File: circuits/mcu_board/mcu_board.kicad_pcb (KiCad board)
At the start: 2 copper layers, 96.3 x 63.9 mm, 44 parts, among them J1 USB_B_Micro, J2 Conn_01x13_Pin, J3 Conn_01x03_Pin, SW1 SW_Push, SW10 SW_Push, SW11 SW_Push, SW12 SW_Push, SW13 SW_Push, SW2 SW_Push, SW3 SW_Push, SW4 SW_Push, SW5 SW_Push, SW6 SW_Push, SW7 SW_Push, SW8 SW_Push, SW9 SW_Push, U1 AMS1117-3.3, U4 STM32F103CBTx, Y1 8MHz

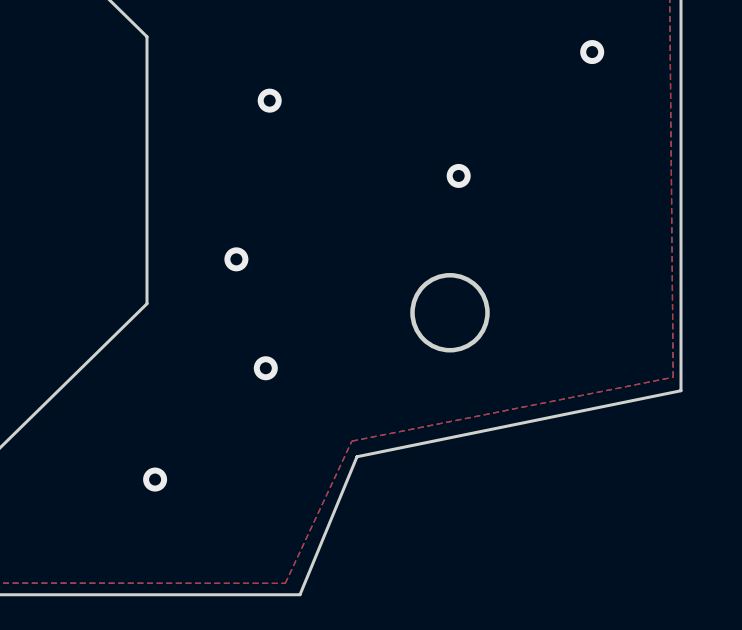
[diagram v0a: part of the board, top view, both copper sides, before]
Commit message: 微调螺丝孔
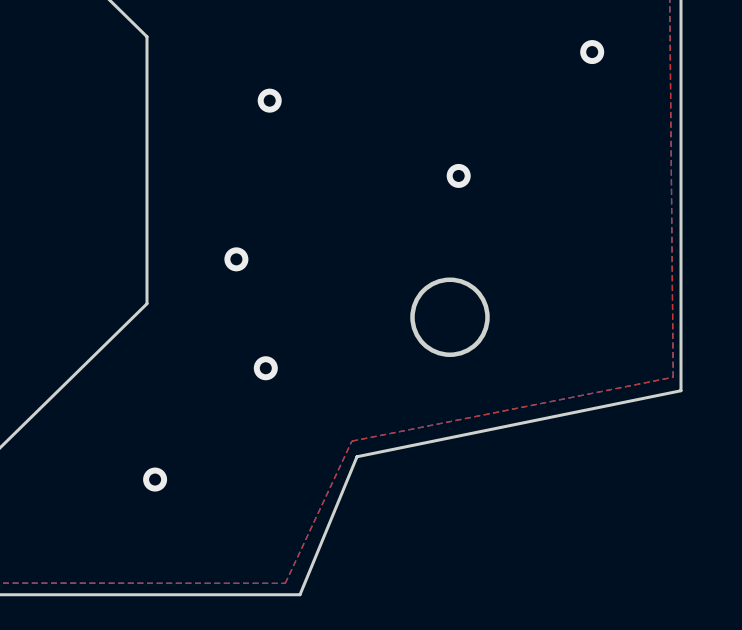
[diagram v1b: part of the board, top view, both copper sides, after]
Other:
- outline, holes or cut-outs redrawn

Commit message: not done
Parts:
- moved C2 7.83 mm to (150.6, 86.8), turned to -90 degrees
- moved C9 4.95 mm to (169.3, 116.7), turned to 90 degrees
- moved C8 4.94 mm to (170.2, 113.4)
- moved Y1 4.00 mm to (166.1, 114.9)
- moved U1 3.72 mm to (149.5, 96.0)
- moved U4 2.38 mm to (150.2, 115.7)
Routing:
- net +3V3: track 385.1 -> 363.9 mm, vias 15 -> 13
- net /BTN_B: track 22.0 -> 3.39 mm
- net Net-(U4-NRST): track 27.2 -> 8.86 mm, vias 2 -> 1
- net /RIGHT_BTN: track 21.5 -> 4.02 mm
- net /LEFT_BTN: track 24.0 -> 13.5 mm
- net VBUS: track 30.3 -> 24.8 mm
- net GND: track 265.9 -> 261.2 mm, vias 133 -> 121
- net /OSC_OUT: track 19.2 -> 16.5 mm, vias 2 -> 1
- net /BTN_LM: track 15.0 -> 17.5 mm
- net /BTN_X: track 58.8 -> 61.2 mm
- net /BTN_RM: track 38.9 -> 41.2 mm
- net Net-(U4-BOOT0): track 18.7 -> 21.0 mm
- net /LEFT_Y: track 13.4 -> 11.0 mm
- net /LEFT_X: track 13.5 -> 11.2 mm
- net /BTN_RB: track 43.8 -> 46.2 mm
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
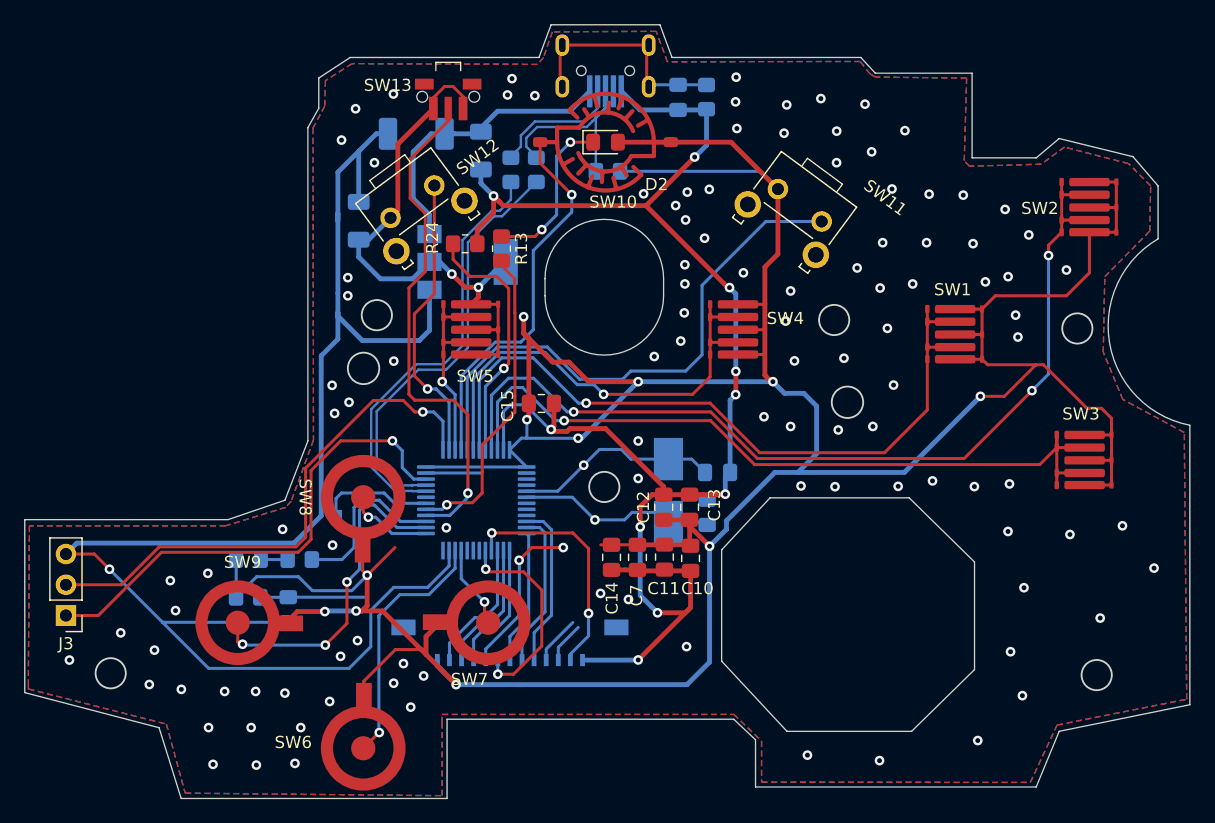
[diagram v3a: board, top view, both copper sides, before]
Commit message: 优化元件位置,防止外壳挤压
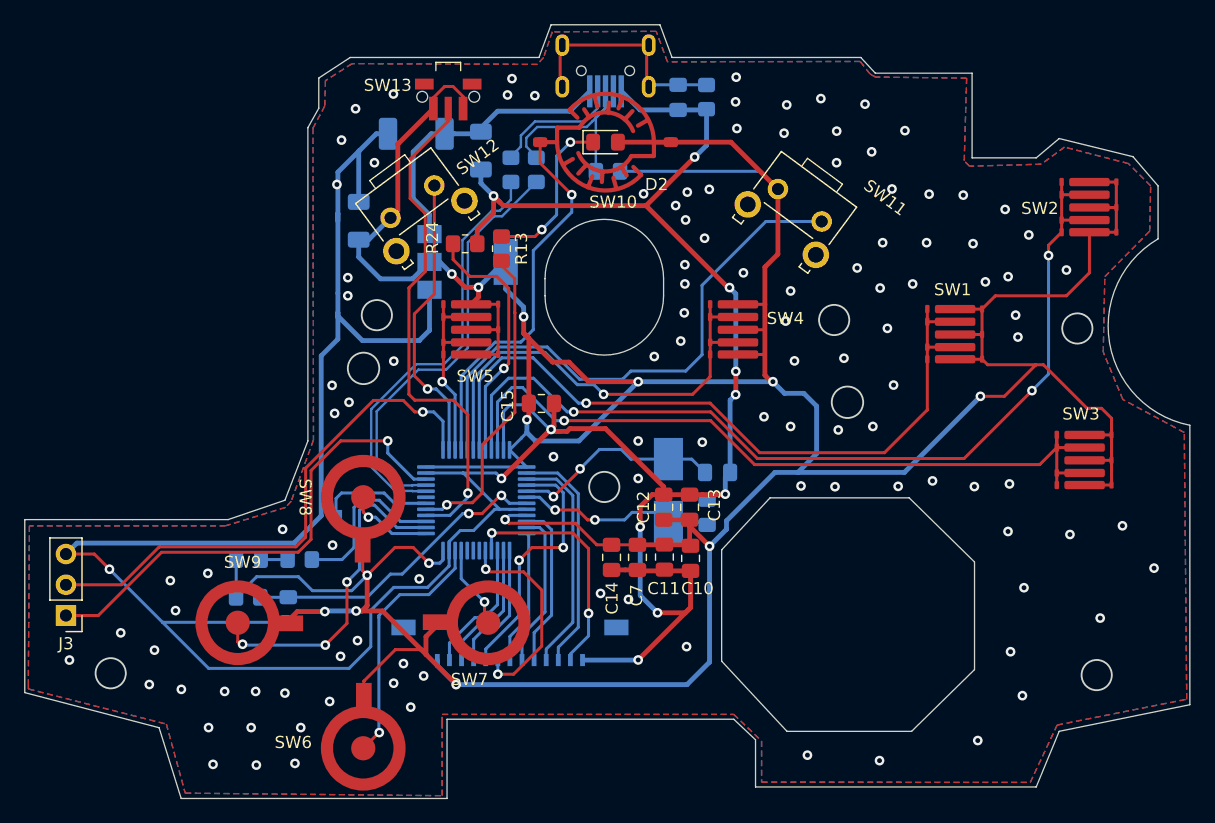
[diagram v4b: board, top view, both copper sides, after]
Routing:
- net +3V3: track 363.9 -> 385.0 mm, vias 13 -> 14
- net GND: track 261.2 -> 282.2 mm, vias 121 -> 126
- net Net-(U4-NRST): track 8.86 -> 25.8 mm, vias 1 -> 2
- net /BTN_B: track 3.39 -> 19.4 mm
- net /RIGHT_BTN: track 4.02 -> 18.9 mm
- net /LEFT_BTN: track 13.5 -> 21.3 mm
- net /OSC_IN: track 17.0 -> 17.4 mm, vias 1 -> 2
- net /OSC_OUT: track 16.5 -> 16.4 mm, vias 1 -> 2

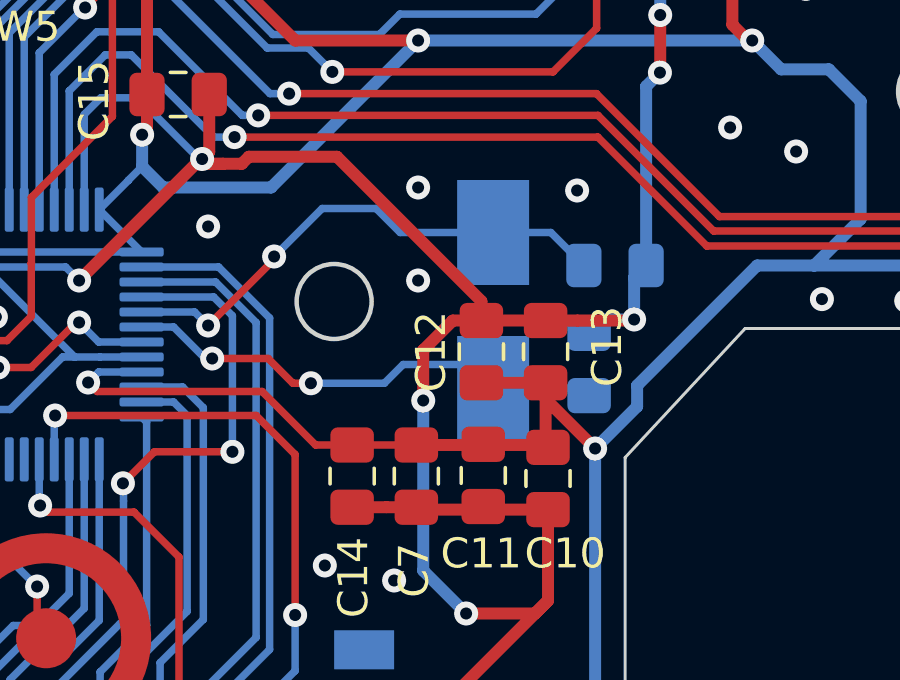
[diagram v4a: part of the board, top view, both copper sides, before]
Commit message: 晶振下移一点
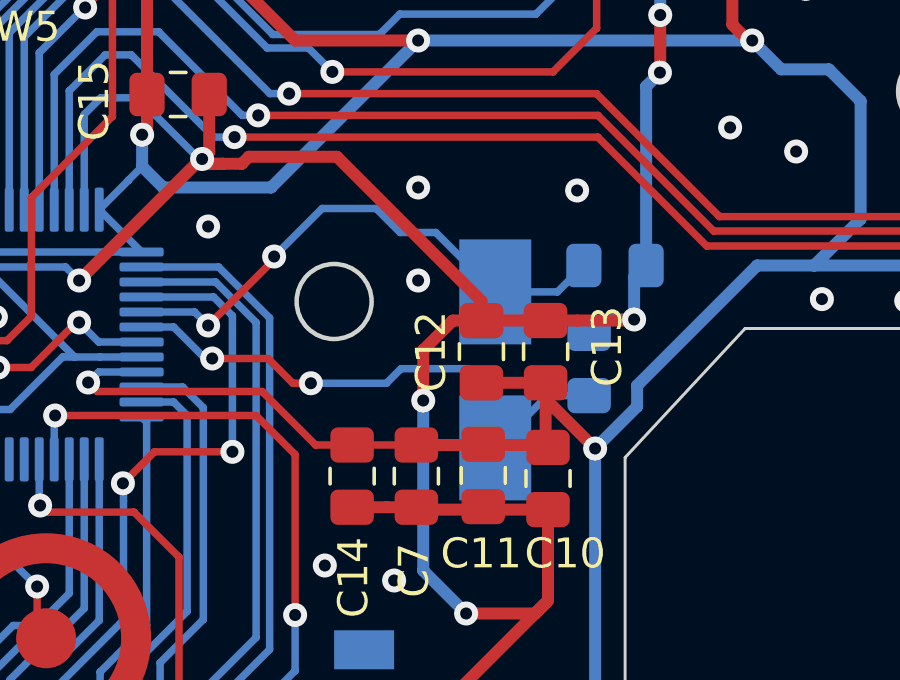
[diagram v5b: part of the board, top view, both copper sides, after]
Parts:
- moved Y1 1.98 mm to (166.2, 116.9)
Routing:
- net /OSC_OUT: track 16.4 -> 19.1 mm
- net /OSC_IN: track 17.4 -> 18.1 mm

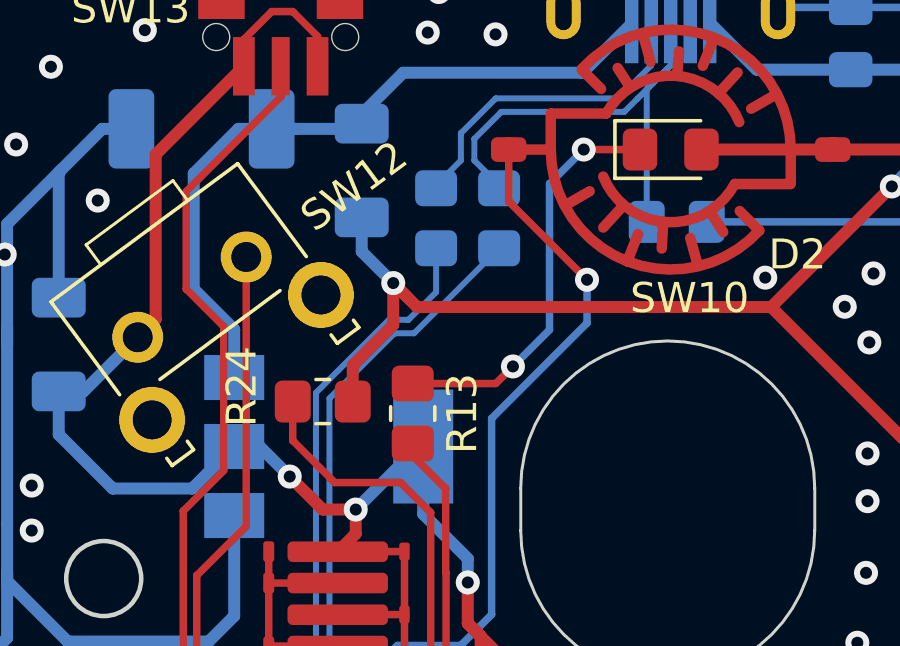
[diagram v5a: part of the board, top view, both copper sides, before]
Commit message: 微调电阻位置
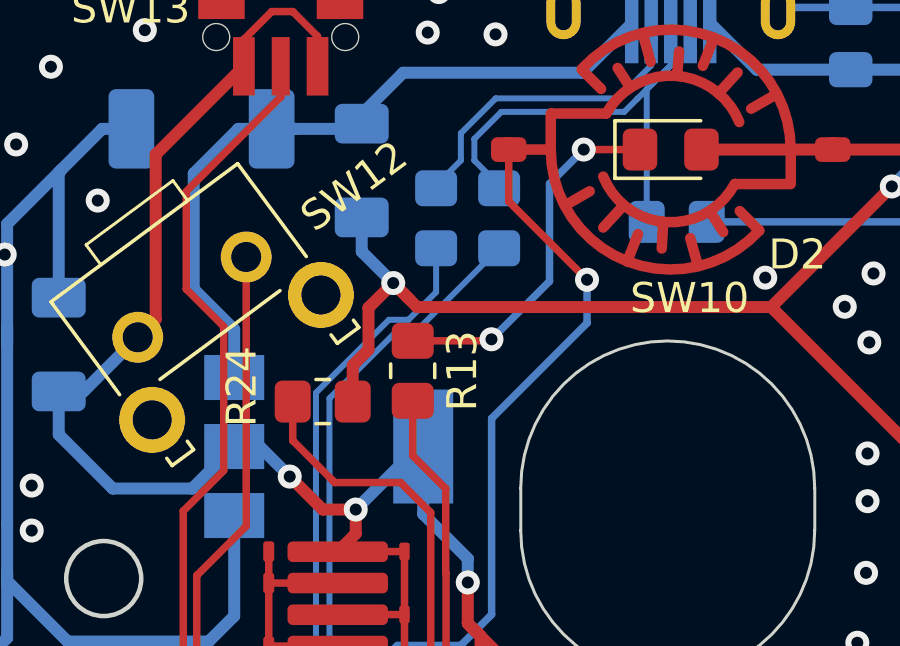
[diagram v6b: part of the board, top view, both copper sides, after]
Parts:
- moved R13 1.43 mm to (152.3, 93.5)
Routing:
- net /LED2: track 25.5 -> 27.3 mm
- net Net-(D2-K): track 13.7 -> 12.3 mm

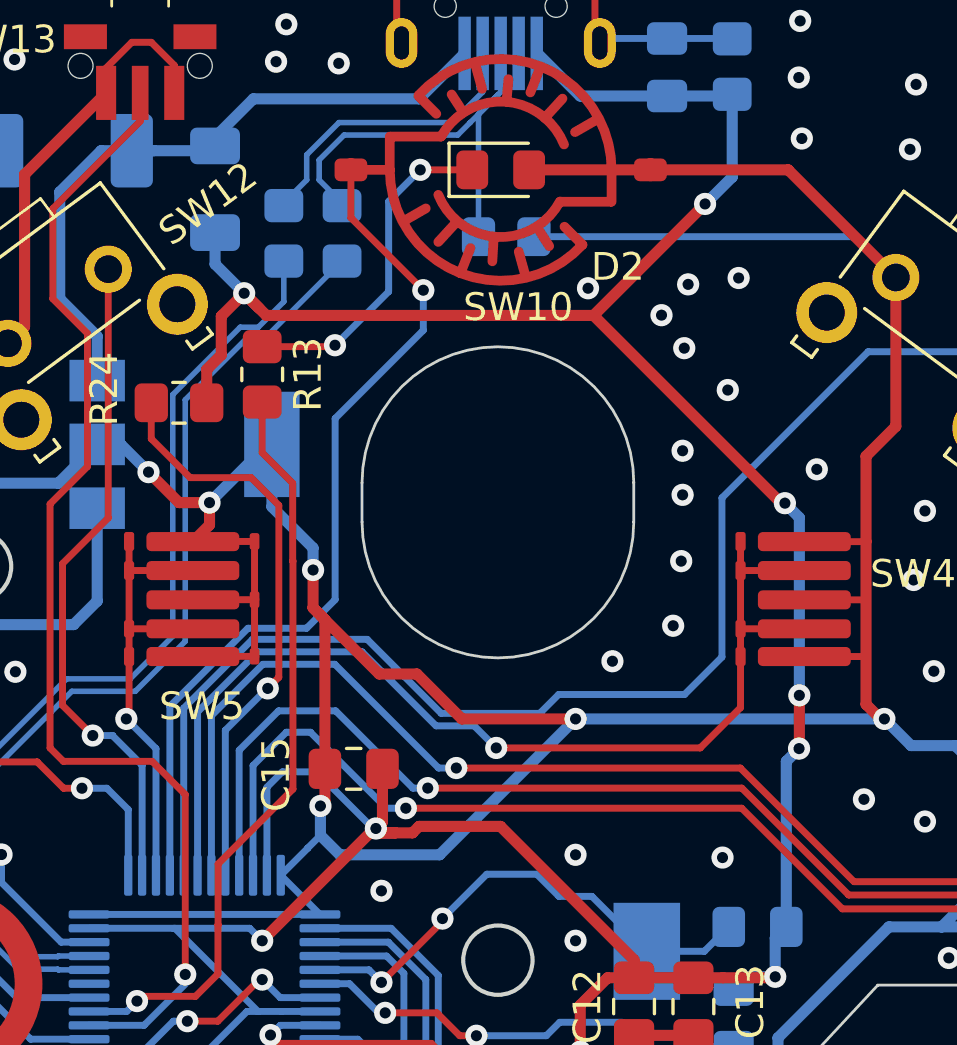
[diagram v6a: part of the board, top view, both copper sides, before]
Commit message: 微调电阻位置
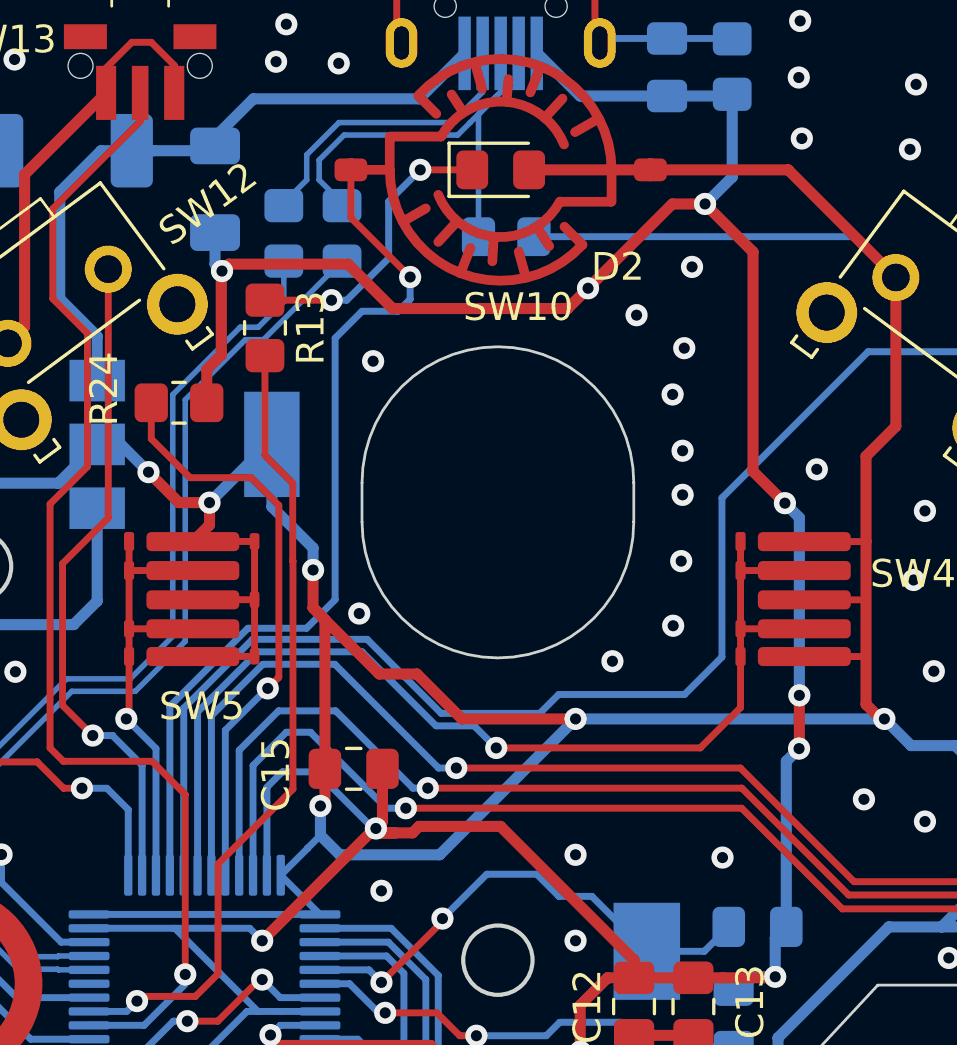
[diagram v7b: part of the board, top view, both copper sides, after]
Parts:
- moved R13 1.68 mm to (152.4, 91.8)
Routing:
- net GND: track 282.2 -> 284.3 mm, vias 126 -> 127
- net Net-(D2-K): track 12.3 -> 10.6 mm
- net /LED2: track 27.3 -> 29.0 mm

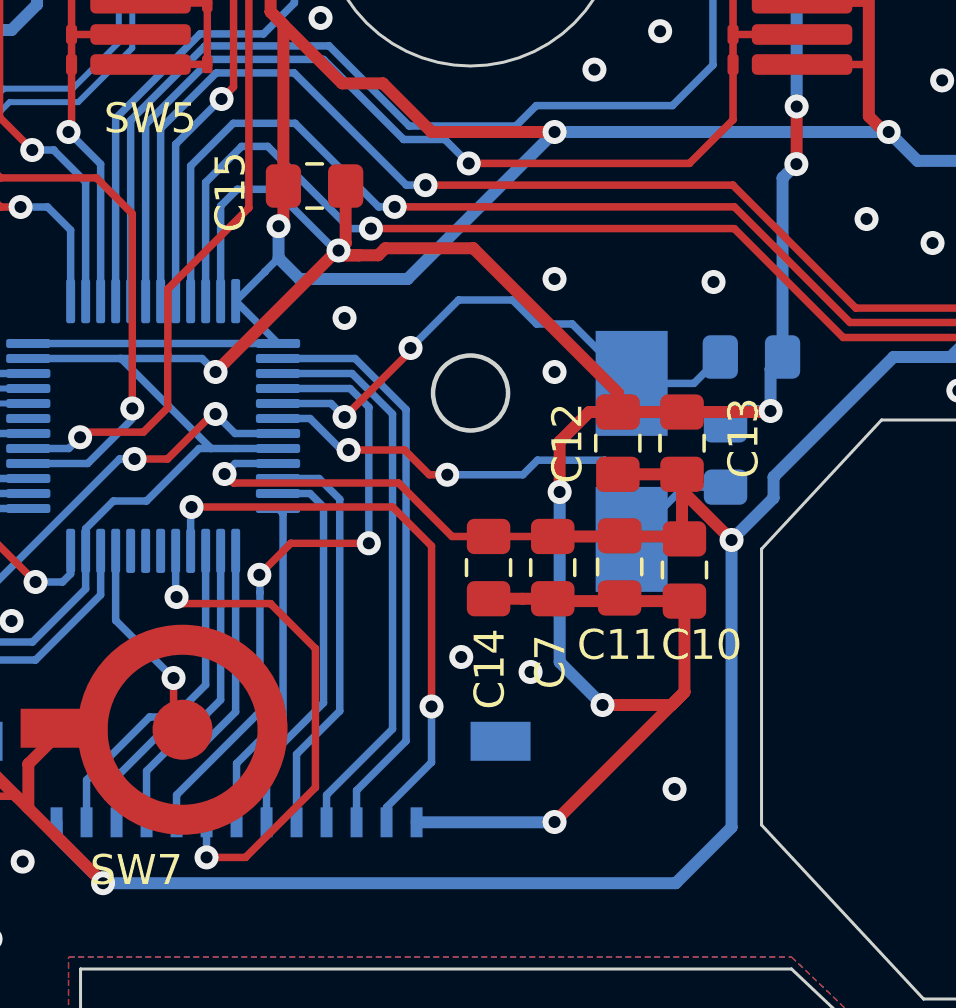
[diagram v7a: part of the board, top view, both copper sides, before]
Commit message: 改电容位置,避免碰到遥感帽
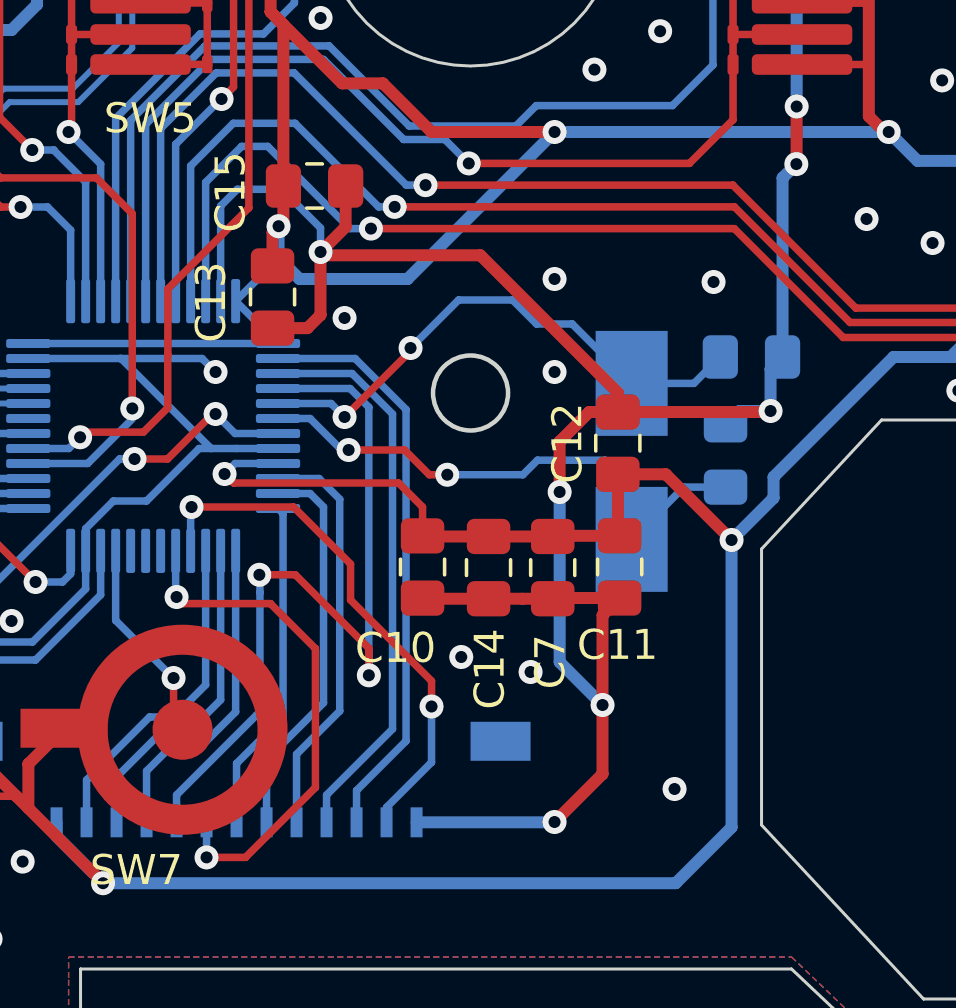
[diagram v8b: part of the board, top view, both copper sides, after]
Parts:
- moved C13 14.5 mm to (154.2, 111.4), turned to -90 degrees
- moved C10 8.73 mm to (159.2, 120.4)
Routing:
- net /LEFT_BTN: track 21.3 -> 27.2 mm
- net GND: track 284.3 -> 278.8 mm
- net /MOTOR2: track 19.8 -> 17.9 mm
- net +3V3: track 385.0 -> 384.3 mm
